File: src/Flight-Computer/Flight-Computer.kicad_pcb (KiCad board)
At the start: 4 copper layers, 93.7 x 43.7 mm, 111 parts, among them J1 Jumper_NO, J2 Jumper_NO, P1 647676-2, P10 Micro_SD_Card, P2 1546551-2, P3 3220-20-0200-00, P4 440054-3, P5 440054-3, P6 440054-3, P7 440054-3, P8 USB, P9 CONN_1984659_PXC, Q1 QS5U17TR, Q2 QS5U17TR, Q3 QS5U17TR, Q4 QS5U17TR, Q5 QS5U17TR, Q6 QS5U17TR, U1 STM32H750VBTx, U10 TS391IYLT, U11 TS391IYLT, U12 BMM150, U2 LMS8117AMP-3.3_NOPB, U3 BMI323_BOS, U4 MAX-8C-0-10, U5 BMP390, U6 SST25VF040B-50-4I-S2AE-T, U7 RFM95W-868S2, U8 CP2102-GMR(QFN28), U9 TS391IYLT, Y1 ECS-240-18-33-JGN-TR

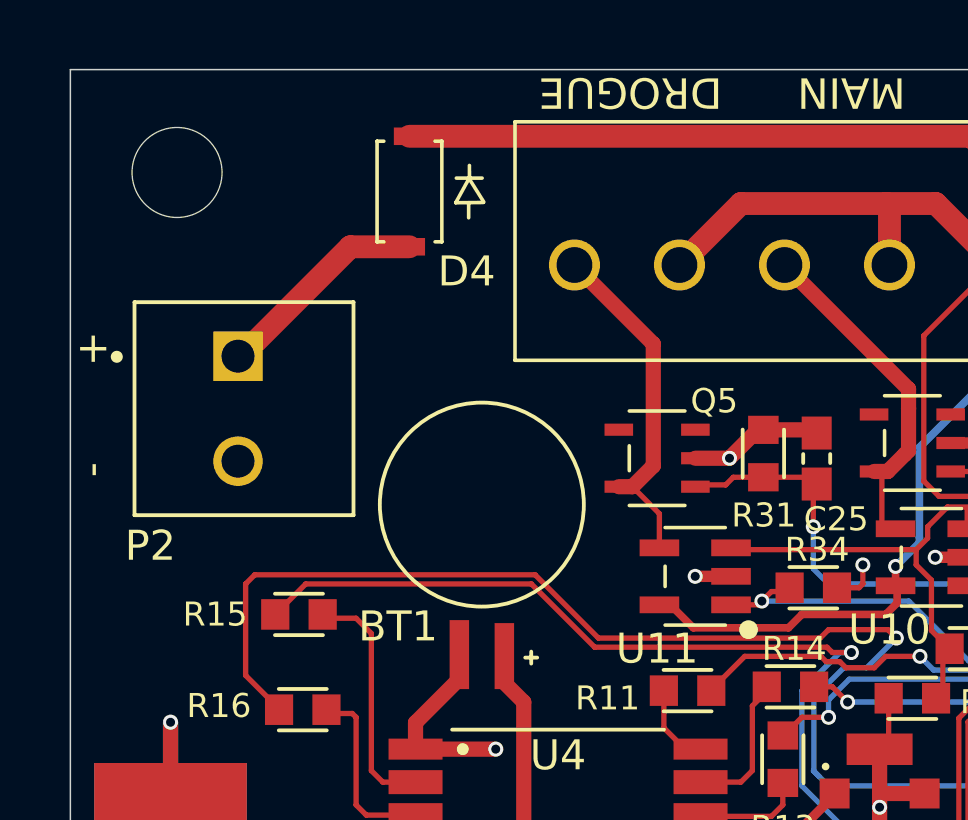
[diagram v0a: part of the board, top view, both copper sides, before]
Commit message: added ignition comparator pull down resistors
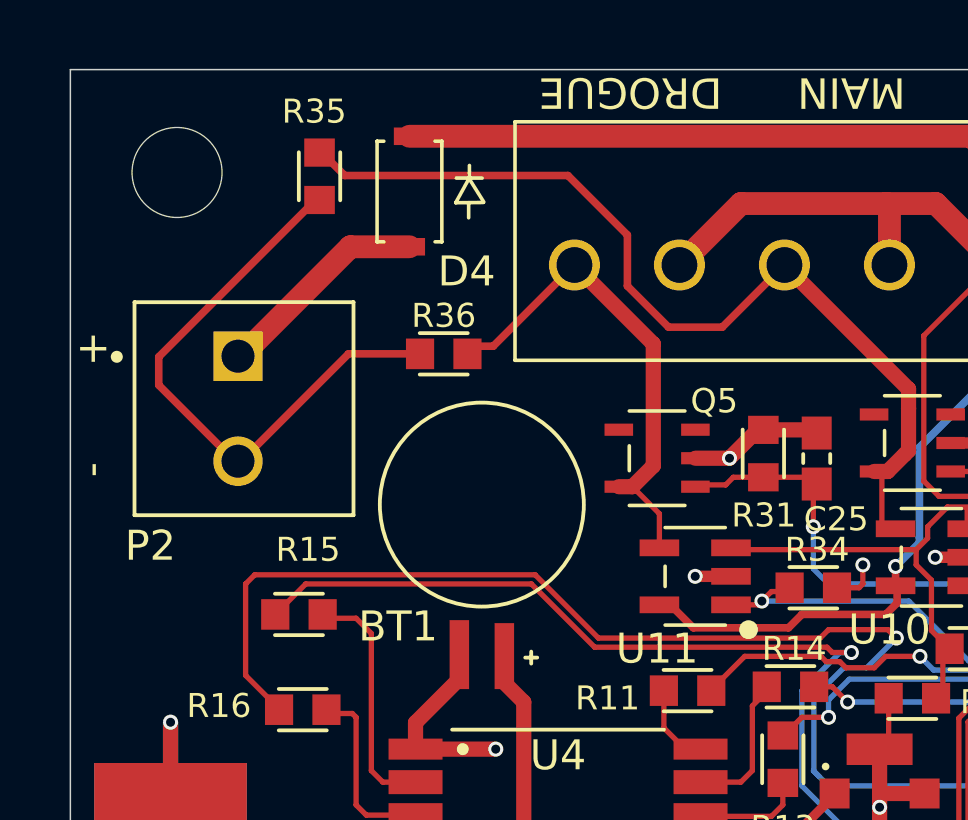
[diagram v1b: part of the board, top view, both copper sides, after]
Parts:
- added R35: 10k, Flight-Computer:RES_0603, F.Cu at (101.3, 61.5)
- added R36: 10k, Flight-Computer:RES_0603, F.Cu at (105.4, 67.4)
- P9: value CONN_1984659_PXC -> 1984659
- U3: value BMI323_BOS -> BMI323
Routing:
- net Earth: track 216.8 -> 236.5 mm
- net Net-(P9-Pad4): track 11.6 -> 31.0 mm
- net Net-(P9-Pad6): track 11.7 -> 16.3 mm
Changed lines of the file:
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@@
     )
   )
+  (footprint "Flight-Computer:RES_0603" (layer "F.Cu")
+    (at 101.2698 61.468 90)
+    (descr "<b>RESISTOR</b>")
+    (property "Field2" "USB")
+    (property "Field3" "Flash")
+    (property "Field4" "Parachute Deployment")
+    (property "Field5" "Wireless")
+    (property "Field6" "Buzzer")
+    (property "Sheetfile" "peripherals.kicad_sch")
+    (property "Sheetname" "Peripherals")
+    (attr through_hole)
+    (fp_text reference "R35" (at 2.159 -0.1778 180) (layer "F.SilkS")
+      (effects (font (size 0.8 0.8) (thickness 0.0762)))
+    )
+    (fp_text value "10k" (at 0 1.2954 90) (layer "F.Fab")
+      (effects (font (size 0.414772 0.414772) (thickness 0.0762)))
+    )
+    (fp_line (start -0.8 -0.69) (end 0.8 -0.69) (layer "F.SilkS") (width 0.127))
+    (fp_line (start -0.8 0.69) (end 0.8 0.69) (layer "F.SilkS") (width 0.127))
+    (fp_line (start -1.51 0.76) (end -1.51 -0.76) (layer "F.CrtYd") (width 0.05))
+    (fp_line (start -1.51 -0.76) (end 1.51 -0.76) (layer "F.CrtYd") (width 0.05))
+    (fp_line (start 1.51 -0.76) (end 1.51 0.76) (layer "F.CrtYd") (width 0.05))
+    (fp_line (start 1.51 0.76) (end -1.51 0.76) (layer "F.CrtYd") (width 0.05))
+    (fp_line (start -0.9 0.5) (end 0.9 0.5) (layer "F.Fab") (width 0.127))
+    (fp_line (start -0.9 -0.5) (end -0.9 0.5) (layer "F.Fab") (width 0.127))
+    (fp_line (start -0.9 -0.5) (end 0.9 -0.5) (layer "F.Fab") (width 0.127))
+    (fp_line (start 0.9 -0.5) (end 0.9 0.5) (layer "F.Fab") (width 0.127))
+    (pad "1" smd rect (at -0.79 0 90) (size 0.94 1.02) (layers "F.Cu" "F.Paste" "F.Mask")
+      (net 1 "Earth") (pintype "passive"))
+    (pad "2" smd rect (at 0.79 0 90) (size 0.94 1.02) (layers "F.Cu" "F.Paste" "F.Mask")
+      (net 163 "Net-(P9-Pad4)") (pintype "passive"))
+    (model "/home/olsport/Documents/SDR/PCB/Flight-Computer/CAD/3Dfiles/RES_0603.step"
+      (offset (xyz 0 0 0))
+      (scale (xyz 1 1 1))
+      (rotate (xyz 0 0 0))
+    )
+  )
   (footprint "Flight-Computer:SM5819PL-TP" (layer "F.Cu")
     (at 168.783 64.77)
@@
     )
   )
+  (footprint "Flight-Computer:RES_0603" (layer "F.Cu")
+    (at 105.41 67.3862)
+    (descr "<b>RESISTOR</b>")
+    (property "Field2" "USB")
+    (property "Field3" "Flash")
+    (property "Field4" "Parachute Deployment")
+    (property "Field5" "Wireless")
+    (property "Field6" "Buzzer")
+    (property "Sheetfile" "peripherals.kicad_sch")
+    (property "Sheetname" "Peripherals")
+    (attr through_hole)
+    (fp_text reference "R36" (at 0 -1.27) (layer "F.SilkS")
+      (effects (font (size 0.8 0.8) (thickness 0.0762)))
+    )
+    (fp_text value "10k" (at 0 1.2954) (layer "F.Fab")
+      (effects (font (size 0.414772 0.414772) (thickness 0.0762)))
+    )
+    (fp_line (start -0.8 0.69) (end 0.8 0.69) (layer "F.SilkS") (width 0.127))
+    (fp_line (start -0.8 -0.69) (end 0.8 -0.69) (layer "F.SilkS") (width 0.127))
+    (fp_line (start 1.51 -0.76) (end 1.51 0.76) (layer "F.CrtYd") (width 0.05))
+    (fp_line (start -1.51 0.76) (end -1.51 -0.76) (layer "F.CrtYd") (width 0.05))
+    (fp_line (start 1.51 0.76) (end -1.51 0.76) (layer "F.CrtYd") (width 0.05))
+    (fp_line (start -1.51 -0.76) (end 1.51 -0.76) (layer "F.CrtYd") (width 0.05))
+    (fp_line (start -0.9 -0.5) (end 0.9 -0.5) (layer "F.Fab") (width 0.127))
+    (fp_line (start 0.9 -0.5) (end 0.9 0.5) (layer "F.Fab") (width 0.127))
+    (fp_line (start -0.9 0.5) (end 0.9 0.5) (layer "F.Fab") (width 0.127))
+    (fp_line (start -0.9 -0.5) (end -0.9 0.5) (layer "F.Fab") (width 0.127))
+    (pad "1" smd rect (at -0.79 0) (size 0.94 1.02) (layers "F.Cu" "F.Paste" "F.Mask")
+      (net 1 "Earth") (pintype "passive"))
+    (pad "2" smd rect (at 0.79 0) (size 0.94 1.02) (layers "F.Cu" "F.Paste" "F.Mask")
+      (net 63 "Net-(P9-Pad6)") (pintype "passive"))
+    (model "/home/olsport/Documents/SDR/PCB/Flight-Computer/CAD/3Dfiles/RES_0603.step"
+      (offset (xyz 0 0 0))
+      (scale (xyz 1 1 1))
+      (rotate (xyz 0 0 0))
+    )
+  )
   (footprint "Flight-Computer:MM3Z3V3B" (layer "F.Cu")
     (at 162.052 90.424 90)
@@
       (effects (font (size 1 1) (thickness 0.15)))
     )
-    (fp_text value "CONN_1984659_PXC" (at 8.82 6.38) (layer "F.SilkS") hide
+    (fp_text value "1984659" (at 8.82 6.38) (layer "F.SilkS") hide
       (effects (font (size 1 1) (thickness 0.15)))
     )
@@
       (effects (font (size 1 1) (thickness 0.15)))
     )
-    (fp_text value "BMI323_BOS" (at -0.12 -3.67 90) (layer "F.SilkS") hide
+    (fp_text value "BMI323" (at -0.12 -3.67 90) (layer "F.SilkS") hide
       (effects (font (size 1 1) (thickness 0.15)))
     )
@@
     (property "Sheetname" "Navigation and Control")
     (attr through_hole)
-    (fp_text reference "R15" (at 2.794 0 180) (layer "F.SilkS")
+    (fp_text reference "R15" (at -0.3048 2.159 180) (layer "F.SilkS")
       (effects (font (size 0.8 0.8) (thickness 0.0762)))
     )
@@
   (segment (start 181.9326 70.614) (end 183.3072 70.614) (width 0.381) (layer "F.Cu") (net 1))
   (segment (start 160.274 71.501) (end 161.036 70.739) (width 0.1778) (layer "F.Cu") (net 1))
+  (segment (start 101.2698 62.258) (end 101.1402 62.258) (width 0.254) (layer "F.Cu") (net 1))
   (segment (start 135.855 84.039) (end 135.29 84.039) (width 0.127) (layer "F.Cu") (net 1))
   (segment (start 159.0675 64.4525) (end 158.877 64.643) (width 0.762) (layer "F.Cu") (net 1))
@@
   (segment (start 135.001 84.328) (end 135.128 84.328) (width 0.127) (layer "F.Cu") (net 1))
   (segment (start 173.581 75.819) (end 173.581 77.188) (width 0.254) (layer "F.Cu") (net 1))
+  (segment (start 102.235 67.3862) (end 98.552 71.0692) (width 0.254) (layer "F.Cu") (net 1))
   (segment (start 177.634 69.303) (end 177.634 69.938) (width 0.508) (layer "F.Cu") (net 1))
   (segment (start 164.973 65.786) (end 166.116 66.929) (width 0.762) (layer "F.Cu") (net 1))
@@
   (segment (start 137.541 82.296) (end 137.4775 82.2325) (width 0.1778) (layer "F.Cu") (net 1))
   (segment (start 166.116 66.929) (end 169.672 66.929) (width 0.762) (layer "F.Cu") (net 1))
+  (segment (start 101.1402 62.258) (end 95.9104 67.4878) (width 0.254) (layer "F.Cu") (net 1))
   (segment (start 159.512 92.06865) (end 159.512 88.646) (width 0.508) (layer "F.Cu") (net 1))
   (segment (start 170.23735 99.87935) (end 171.196 100.838) (width 0.508) (layer "F.Cu") (net 1))
@@
   (segment (start 157.607 85.344) (end 158.115 85.852) (width 0.254) (layer "F.Cu") (net 1))
   (segment (start 140.97 88.48) (end 140.97 88.519) (width 0.1778) (layer "F.Cu") (net 1))
+  (segment (start 95.9104 68.4276) (end 98.5012 71.0184) (width 0.254) (layer "F.Cu") (net 1))
   (segment (start 126.607001 80.1243) (end 127.2413 80.1243) (width 0.1778) (layer "F.Cu") (net 1))
   (segment (start 137.0838 77.1398) (end 139.4968 77.1398) (width 0.1778) (layer "F.Cu") (net 1))
@@
   (segment (start 157.607 72.517) (end 157.861 72.263) (width 0.1778) (layer "F.Cu") (net 1))
   (segment (start 135.255 84.328) (end 135.128 84.328) (width 0.127) (layer "F.Cu") (net 1))
+  (segment (start 104.62 67.3862) (end 102.235 67.3862) (width 0.254) (layer "F.Cu") (net 1))
   (segment (start 155.067 84.582) (end 155.829 85.344) (width 0.254) (layer "F.Cu") (net 1))
   (segment (start 131.738 81.827) (end 131.8895 81.9785) (width 0.1778) (layer "F.Cu") (net 1))
@@
   (segment (start 175.746 77.683) (end 184.699 77.683) (width 0.762) (layer "F.Cu") (net 1))
   (segment (start 134.239 86.653) (end 134.913 86.653) (width 0.1778) (layer "F.Cu") (net 1))
+  (segment (start 95.9104 67.4878) (end 95.9104 68.4276) (width 0.254) (layer "F.Cu") (net 1))
   (segment (start 135.289 84.294) (end 135.255 84.328) (width 0.127) (layer "F.Cu") (net 1))
   (segment (start 119.9388 82.4992) (end 119.9388 83.3628) (width 0.508) (layer "F.Cu") (net 1))
@@
   (segment (start 111.24565 71.816001) (end 111.698999 71.816001) (width 0.508) (layer "F.Cu") (net 63))
   (segment (start 111.698999 71.816001) (end 112.395 71.12) (width 0.508) (layer "F.Cu") (net 63))
+  (segment (start 107.060147 67.1322) (end 106.299 67.1322) (width 0.254) (layer "F.Cu") (net 63))
+  (segment (start 109.767246 64.425101) (end 107.060147 67.1322) (width 0.254) (layer "F.Cu") (net 63))
   (segment (start 112.5982 73.852999) (end 112.5982 72.715202) (width 0.1778) (layer "F.Cu") (net 63))
   (segment (start 112.395 71.12) (end 112.395 67.056) (width 0.508) (layer "F.Cu") (net 63))
@@
   (segment (start 119.75465 71.308001) (end 120.207999 71.308001) (width 0.508) (layer "F.Cu") (net 163))
   (segment (start 120.015 73.152) (end 120.015 71.374) (width 0.1778) (layer "F.Cu") (net 163))
+  (segment (start 114.695148 66.4972) (end 112.903 66.4972) (width 0.254) (layer "F.Cu") (net 163))
   (segment (start 120.777 70.739) (end 120.904 70.612) (width 0.508) (layer "F.Cu") (net 163))
   (segment (start 120.4722 73.217999) (end 120.080999 73.217999) (width 0.1778) (layer "F.Cu") (net 163))
+  (segment (start 111.5314 65.1256) (end 111.5314 63.4238) (width 0.254) (layer "F.Cu") (net 163))
+  (segment (start 109.5502 61.4426) (end 102.108 61.4426) (width 0.254) (layer "F.Cu") (net 163))
   (segment (start 120.904 68.561854) (end 120.904 69.215) (width 0.508) (layer "F.Cu") (net 163))
   (segment (start 120.904 70.612) (end 120.904 69.215) (width 0.508) (layer "F.Cu") (net 163))
+  (segment (start 111.5314 63.4238) (end 109.5502 61.4426) (width 0.254) (layer "F.Cu") (net 163))
+  (segment (start 112.903 66.4972) (end 111.5314 65.1256) (width 0.254) (layer "F.Cu") (net 163))
+  (segment (start 102.108 61.4426) (end 101.5492 60.8838) (width 0.254) (layer "F.Cu") (net 163))
+  (segment (start 116.767247 64.425101) (end 114.695148 66.4972) (width 0.254) (layer "F.Cu") (net 163))
   (zone (net 1) (net_name "Earth") (layer "In1.Cu") (hatch edge 0.508)
     (connect_pads (clearance 0.2032))

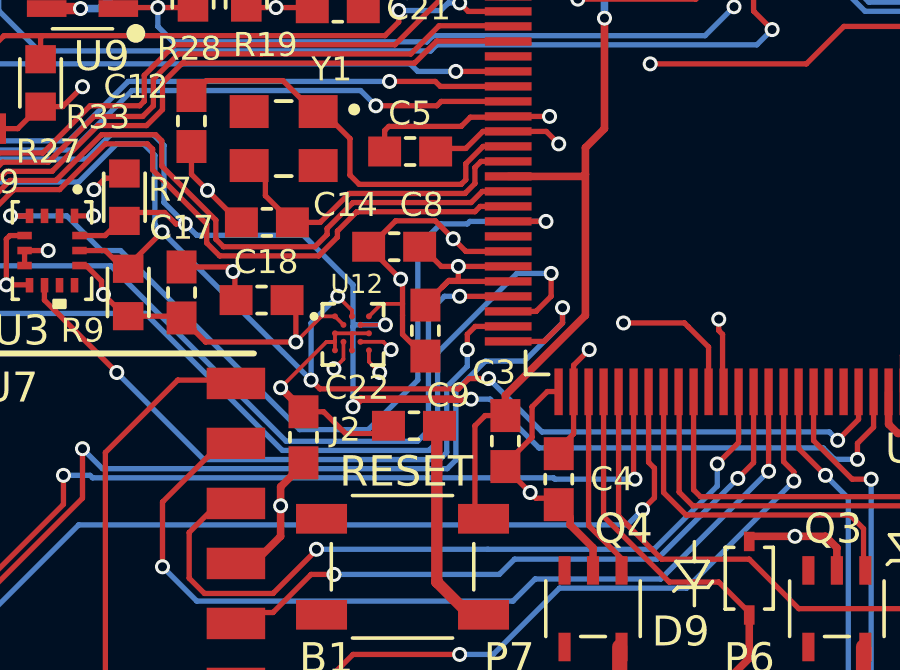
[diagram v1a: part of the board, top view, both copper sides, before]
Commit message: PCB Part 1
Changed first part of flight computer to BMM 350 schematic
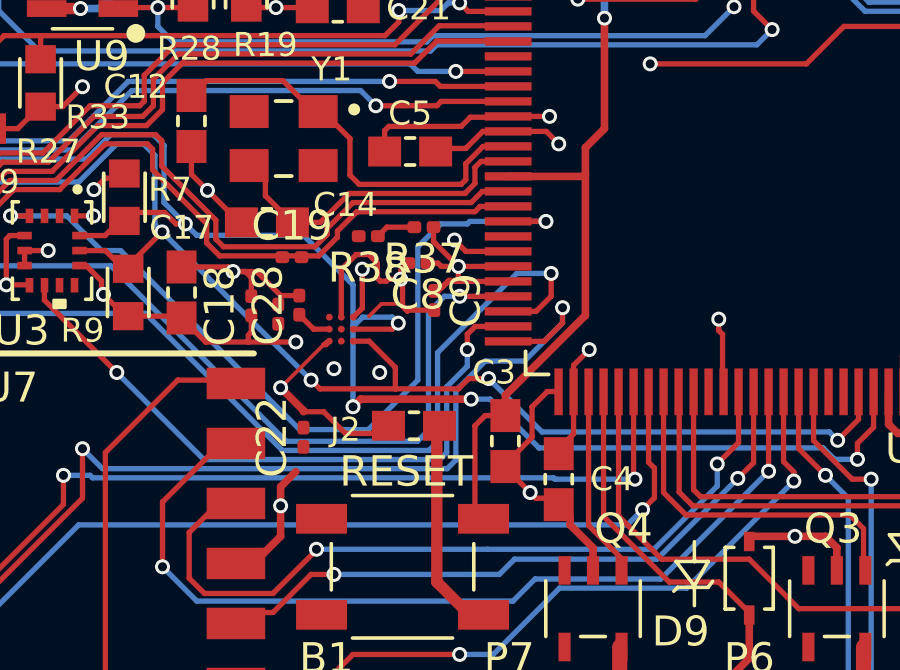
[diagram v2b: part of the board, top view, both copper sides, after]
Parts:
- added C19: 100nF, Capacitor_SMD:C_0201_0603Metric, F.Cu at (133.9, 81.5)
- added C27: 100nF, Capacitor_SMD:C_0201_0603Metric, F.Cu at (133.4, 83.4)
- added C28: 2.2uF, Capacitor_SMD:C_0201_0603Metric, F.Cu at (134.1, 83.1)
- added R37: 1kOhm, Resistor_SMD:R_0201_0603Metric, F.Cu at (138.3, 80.5)
- added R38: 1kOhm, Resistor_SMD:R_0201_0603Metric, F.Cu at (136.4, 80.8)
- C18, C22, C8, C9: footprint Flight-Computer:CAP_0603 -> Capacitor_SMD:C_0201_0603Metric
- U12: value BMM150 -> BMM350; footprint Flight-Computer:BMM150 -> footprints:BGA9_BMM350_BOS
- moved C9 1.05 mm to (138.6, 82.9)
- moved C8 0.96 mm to (138.1, 81.7)
- moved U12 0.43 mm to (135.5, 83.9), turned to -90 degrees
- moved C18 0.39 mm to (132.5, 83.1), turned to 90 degrees
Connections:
- U12 pad A1: 3.3V -> MAG_INT
- U12 pad B2: 3.3V -> Earth
- U12 pad C1: Earth -> +1V8
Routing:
- net MAG_DRDY: track 13.9 -> 0.00 mm, vias 2 -> 0
- net MAG_INT: track 17.9 -> 22.4 mm, vias 2 -> 3
- net Earth: track 236.5 -> 238.3 mm
- net 3.3V: track 94.3 -> 92.7 mm
- net SCL: track 49.8 -> 48.2 mm, vias 6 -> 5
- net SDA: track 53.1 -> 54.5 mm
- net +1V8: track 0.00 -> 1.34 mm

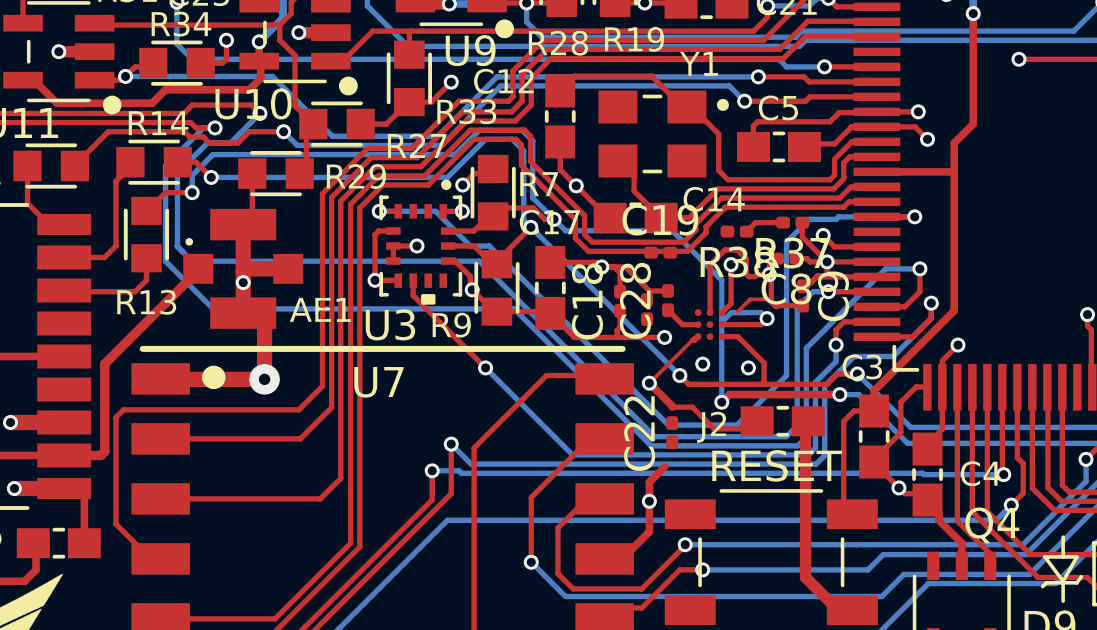
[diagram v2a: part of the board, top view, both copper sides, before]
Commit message: S-85S1A
Added S-85S1A to flight computer schematic
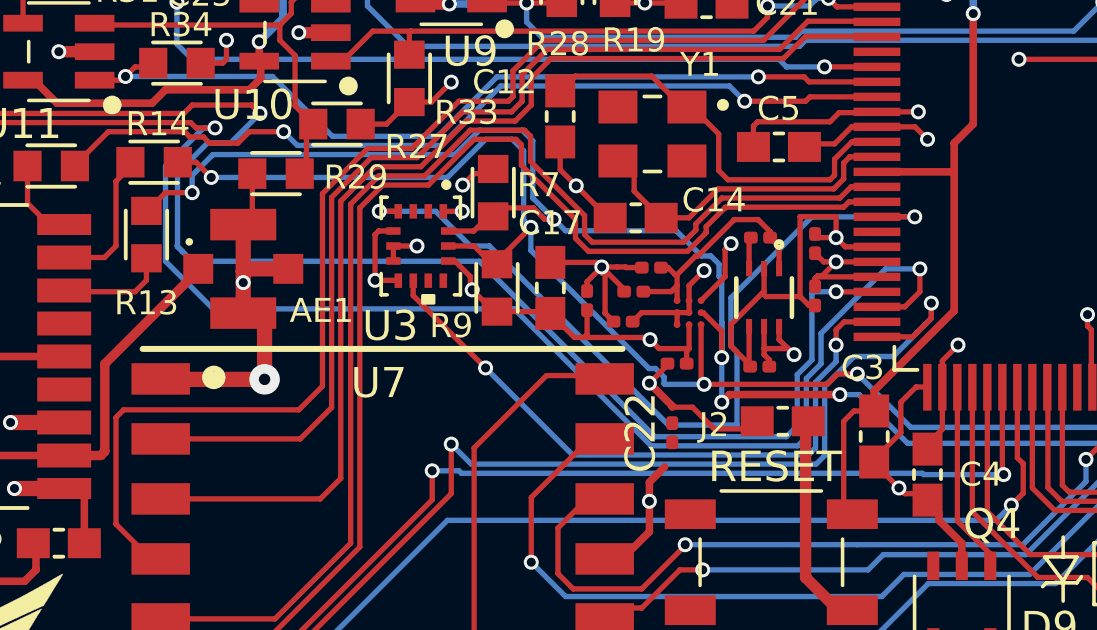
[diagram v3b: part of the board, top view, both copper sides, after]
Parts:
- removed R37, R38: 1kOhm, Resistor_SMD:R_0201_0603Metric
- added C29: 10uF, Capacitor_SMD:C_0201_0603Metric, F.Cu at (137.2, 85.3)
- added C30: 10uF, Capacitor_SMD:C_0201_0603Metric, F.Cu at (133.0, 82.8)
- added L2: 2.2uH, Inductor_SMD:L_0201_0603Metric, F.Cu at (137.2, 81.0)
- added U13: S-85S1AB33-I6T1U, S85S1A:SNT-6A-A-PKG_PG006-A-P-SD-2.1_ABL, F.Cu at (137.3, 83.0)
- moved C19 3.74 mm to (134.4, 85.2), turned to 180 degrees
- moved C28 1.66 mm to (132.6, 83.8), turned to 180 degrees
- moved C27 1.41 mm to (133.5, 82.0), turned to 180 degrees
- moved C18 1.10 mm to (131.4, 83.1)
- moved C8 1.07 mm to (139.0, 81.2), turned to 90 degrees
- moved U12 0.81 mm to (134.8, 83.5)
- moved C9 0.40 mm to (139.0, 82.9)
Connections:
- net +1V8 renamed 1.8V
- C19 pad 1: +3.3V -> 3.3V
- U12 pad B3: +3.3V -> 3.3V
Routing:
- net Earth: track 238.3 -> 245.1 mm
- net 1.8V: track 1.34 -> 8.09 mm
- net 3.3V: track 92.7 -> 95.7 mm
- net Net-(U13-SW): track 0.00 -> 1.06 mm
- net MAG_INT: track 22.4 -> 21.4 mm, vias 3 -> 2
